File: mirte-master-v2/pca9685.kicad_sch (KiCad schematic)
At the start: 1 part, among them J10 pca9685

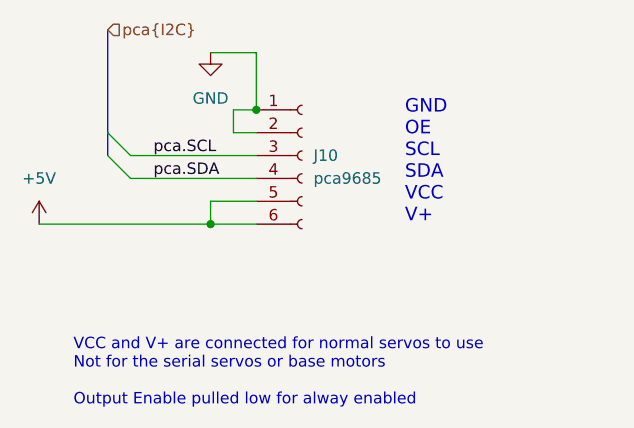
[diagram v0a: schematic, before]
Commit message: integrated the ina226 in the pcb layout
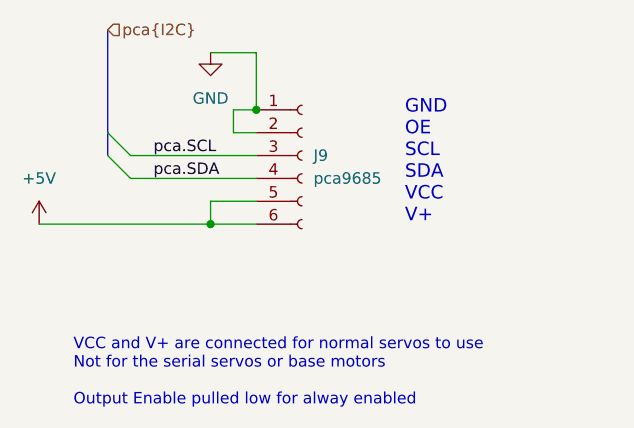
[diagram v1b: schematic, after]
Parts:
- renumbered J10 to J9
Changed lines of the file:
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@@
 		(dnp no)
 		(fields_autoplaced yes)
-		(property "Reference" "J10"
+		(property "Reference" "J9"
 			(at 148.59 83.82 0)
 			(effects
@@
 			(project "mirte-master"
 				(path "/19794465-0368-488c-958e-83b02754ebd6/8cd758b8-bad9-4a6e-8615-cb9455855236"
-					(reference "J10")
+					(reference "J9")
 					(unit 1)
 				)
